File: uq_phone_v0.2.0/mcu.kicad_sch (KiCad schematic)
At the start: 41 parts, among them J6 Conn_ARM_SWD_TagConnect_TC2030, J7 559092474, J9 559092474, Q1 MMBT3904LP-7, Q2 MMBT3904LP-7, U17 TXU0204DTRR, U18 TXU0304DTRR, U19 TXU0104DTRR, U20 TXU0104DTRR, U5 TCA9509MRVHR, U6 STM32H723VGHx

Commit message: Regulator EN-controlled soft power latch prototype
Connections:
- net PWR_HOLD: now reaches U6.G5 (PB2)
- net PB_PWR renamed PWR_BUTTON_SENSE
- no-connect marks 16 -> 15

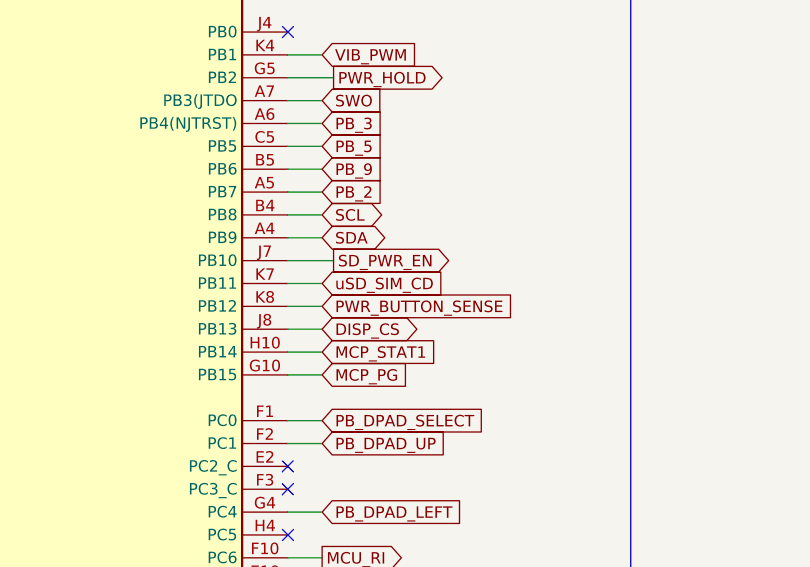
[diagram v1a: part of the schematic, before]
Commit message: Add shared tray detect for MCU and RC7620 SIM detection
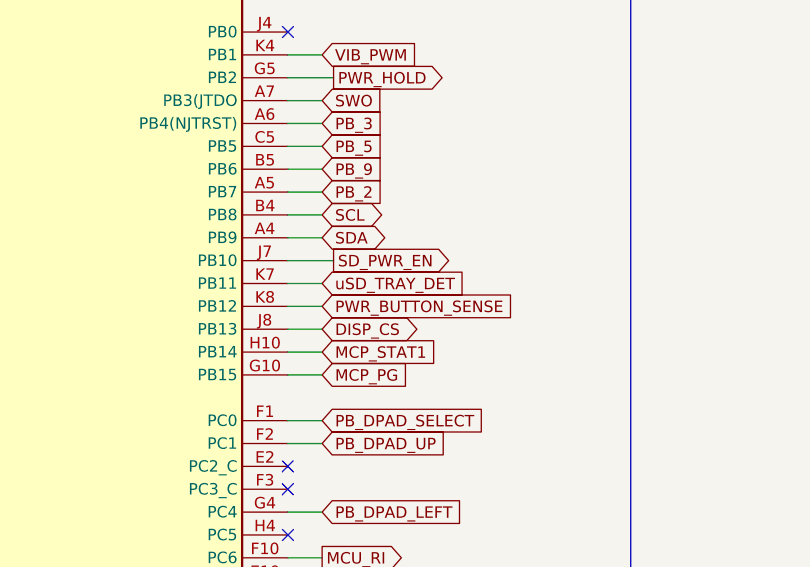
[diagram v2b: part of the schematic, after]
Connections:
- net uSD_SIM_CD renamed uSD_TRAY_DET

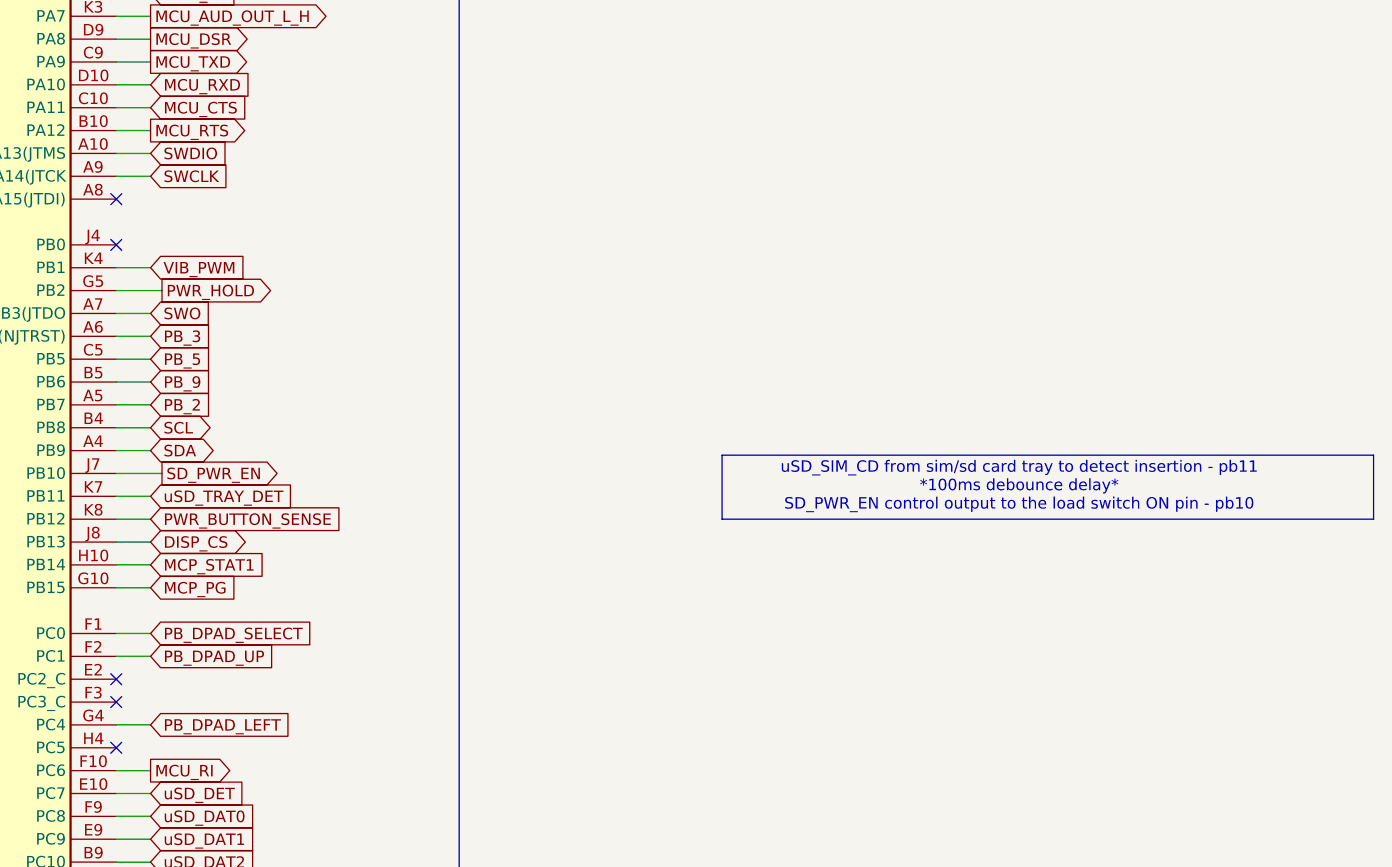
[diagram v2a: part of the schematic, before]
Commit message: Add soft power switch and update PCB design
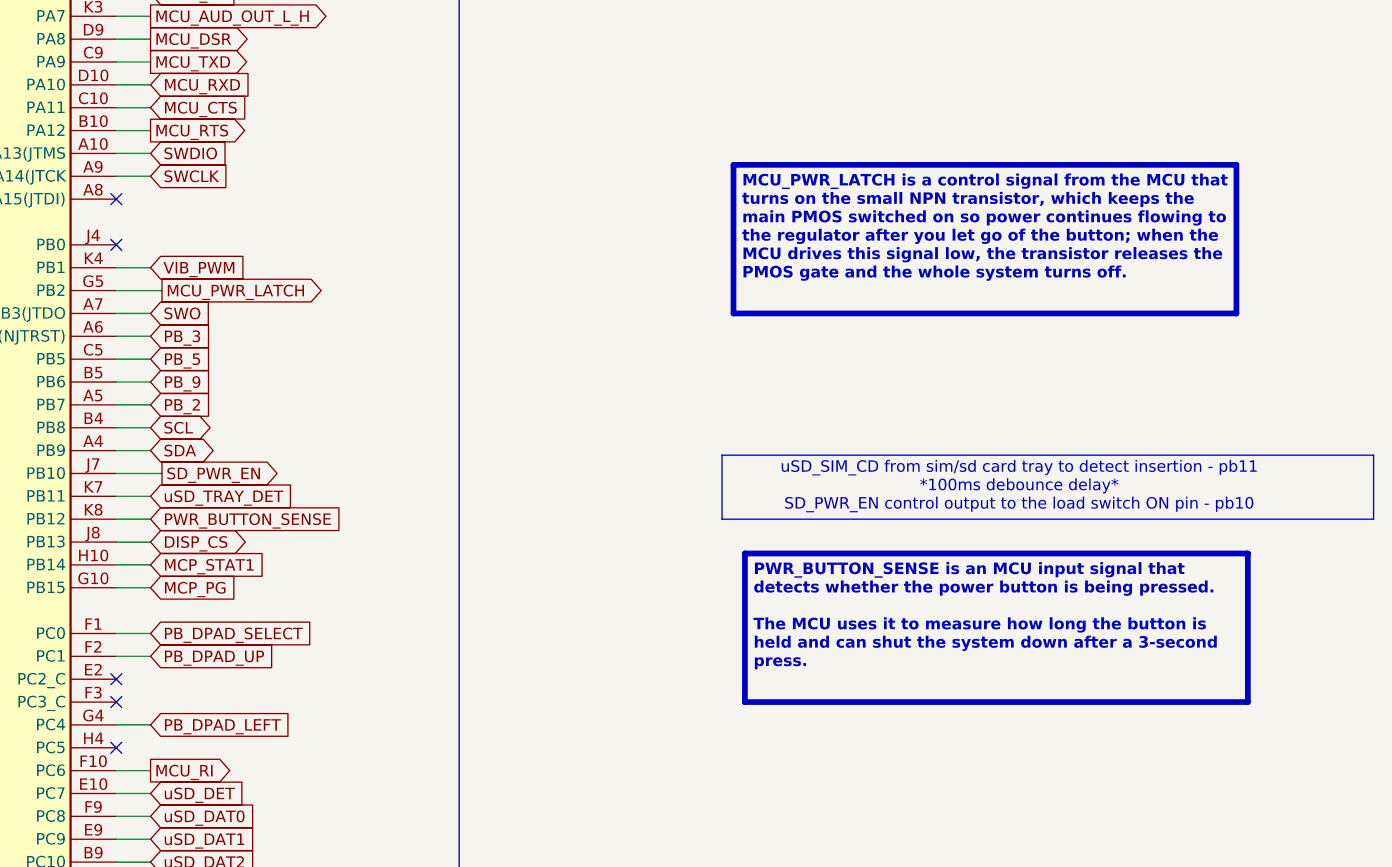
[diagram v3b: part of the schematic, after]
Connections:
- net PWR_HOLD renamed MCU_PWR_LATCH

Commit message: Fix KiCad libraries and update soft power circuit
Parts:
- Q2: footprint MMBT3904LP-7:DFN101X61X53-3N -> MMBT3904LP-7:MMBT3904LP7

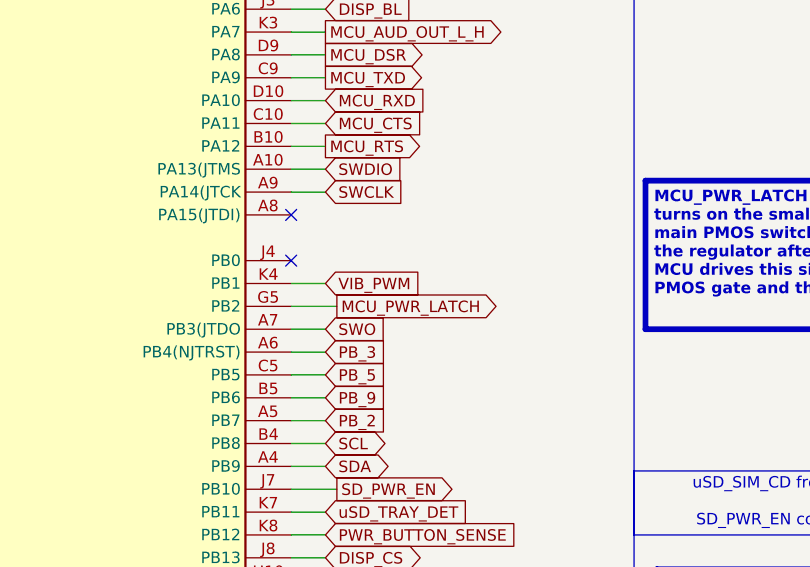
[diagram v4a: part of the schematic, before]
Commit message: Route soft power switch
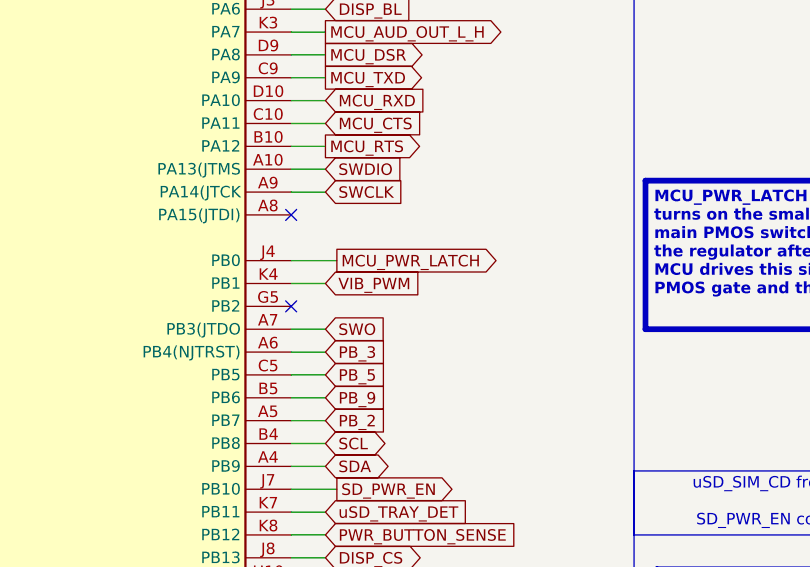
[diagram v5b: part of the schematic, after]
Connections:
- net MCU_PWR_LATCH: now also U6.J4 (PB0); no longer U6.G5 (PB2)

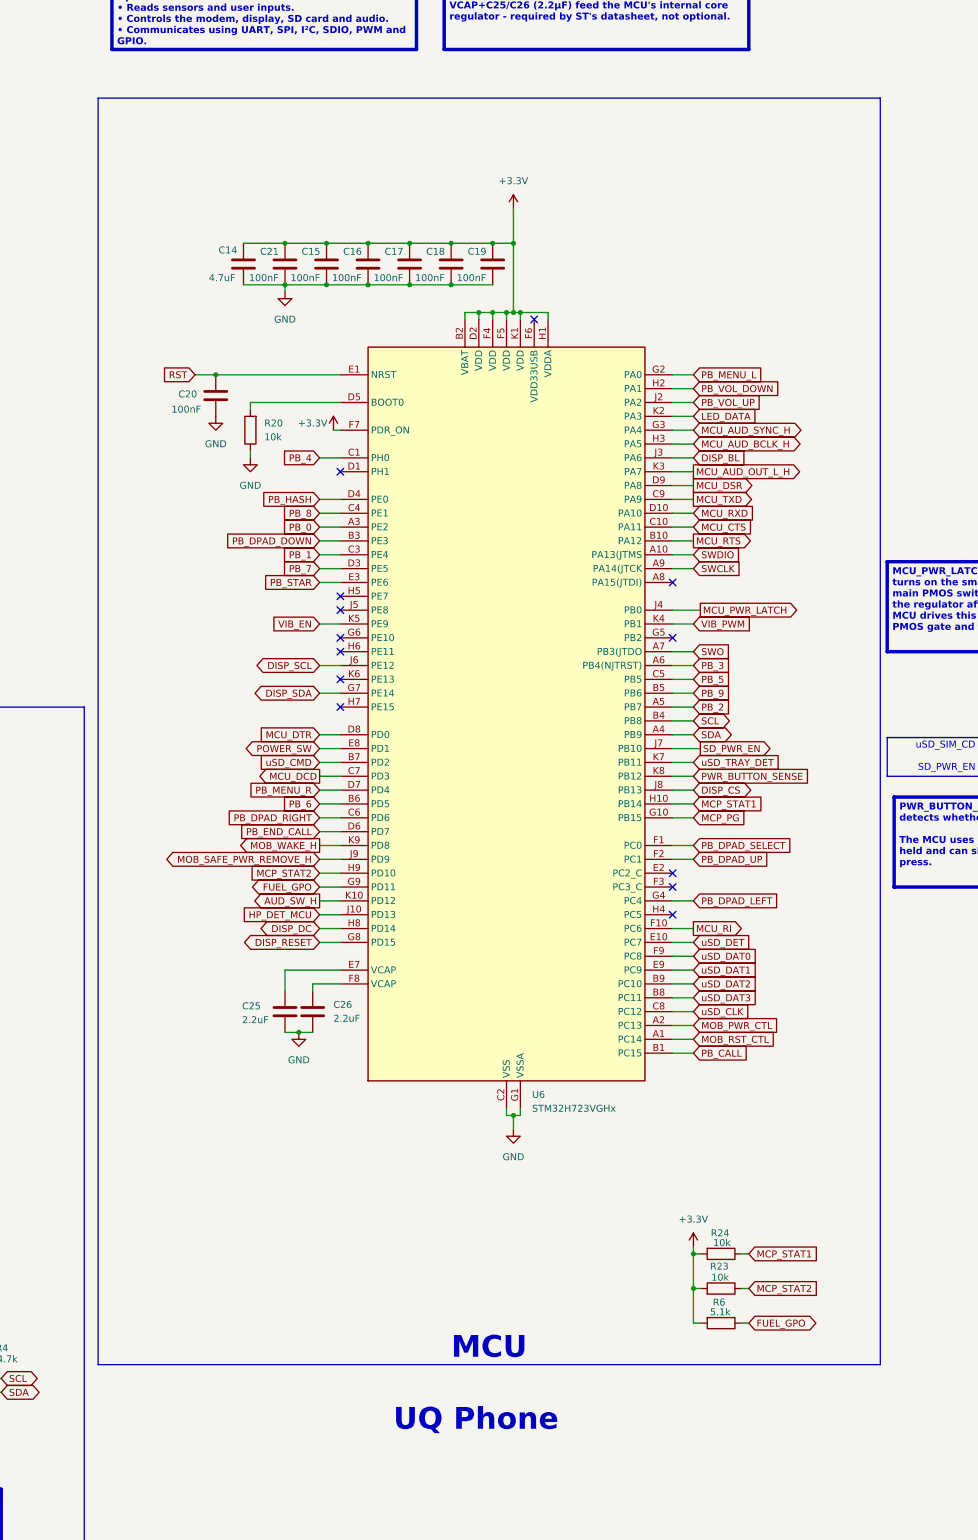
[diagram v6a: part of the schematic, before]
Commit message: Add GPIO expander and 16-bit FMC display schematic
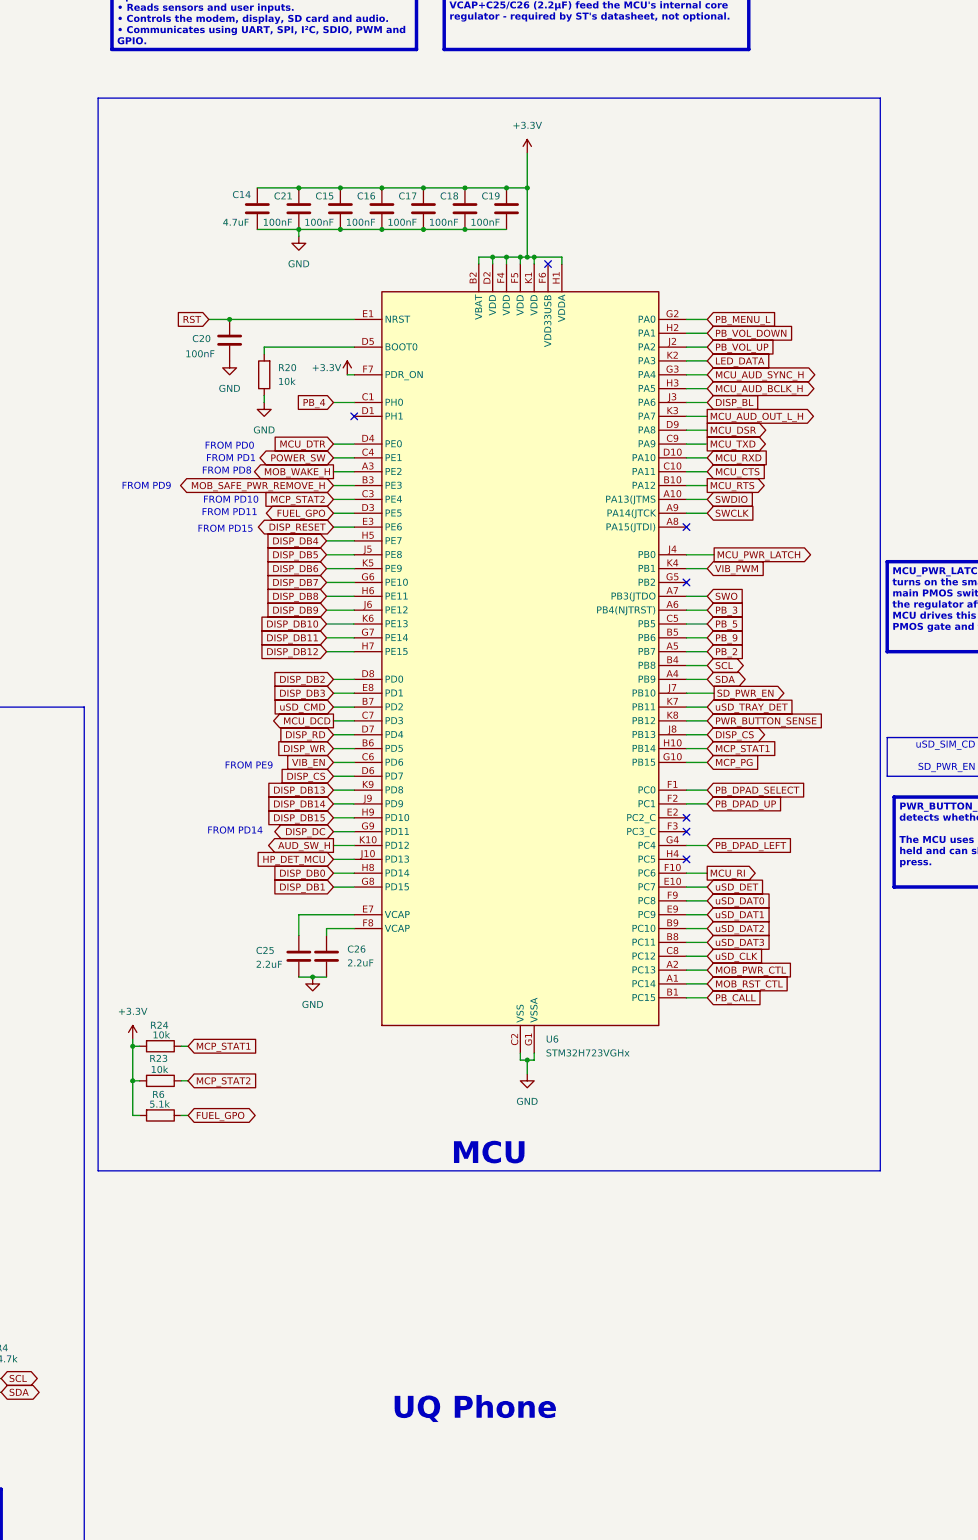
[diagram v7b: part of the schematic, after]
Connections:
- net PB_0 is gone; now on net MOB_WAKE_H: U6.A3 (PE2)
- net PB_1 is gone; now on net MCP_STAT2: U6.C3 (PE4)
- net PB_7 is gone; now on net FUEL_GPO: U6.D3 (PE5)
- net PB_8 is gone; now on net POWER_SW: U6.C4 (PE1)
- net PB_DPAD_DOWN is gone; now on net MOB_SAFE_PWR_REMOVE_H: U6.B3 (PE3)
- net PB_DPAD_RIGHT is gone; now on net VIB_EN: U6.C6 (PD6)
- net PB_END_CALL is gone; now on net DISP_CS: U6.D6 (PD7)
- net PB_HASH is gone; now on net MCU_DTR: U6.D4 (PE0)
- net PB_STAR is gone; now on net DISP_RESET: U6.E3 (PE6)
- net DISP_DC: now also U6.G9 (PD11); no longer U6.H8 (PD14)
- net DISP_RESET: no longer U6.G8 (PD15)
- net FUEL_GPO: no longer U6.G9 (PD11)
- net MCP_STAT2: no longer U6.H9 (PD10)
- net MCU_DTR: no longer U6.D8 (PD0)
- net MOB_SAFE_PWR_REMOVE_H: no longer U6.J9 (PD9)
- net MOB_WAKE_H: no longer U6.K9 (PD8)
- net POWER_SW: no longer U6.E8 (PD1)
- net VIB_EN: no longer U6.K5 (PE9)
- net DISP_DB7: now reaches U6.G6 (PE10)
- net DISP_DB4: now reaches U6.H5 (PE7)
- net DISP_DB8: now reaches U6.H6 (PE11)
- net DISP_DB12: now reaches U6.H7 (PE15)
- net DISP_DB5: now reaches U6.J5 (PE8)
- net DISP_DB10: now reaches U6.K6 (PE13)
- net DISP_SCL renamed DISP_DB9
- net DISP_SDA renamed DISP_DB11
- net PB_6 renamed DISP_WR
- net PB_MENU_R renamed DISP_RD
- new net DISP_DB0: U6.H8 (PD14)
- new net DISP_DB1: U6.G8 (PD15)
- new net DISP_DB13: U6.K9 (PD8)
- new net DISP_DB14: U6.J9 (PD9)
- new net DISP_DB15: U6.H9 (PD10)
- new net DISP_DB2: U6.D8 (PD0)
- new net DISP_DB3: U6.E8 (PD1)
- new net DISP_DB6: U6.K5 (PE9)
- no-connect marks 15 -> 9
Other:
- note added: "FROM PD0"
- note added: "FROM PD1"
- note added: "FROM PD10"
- note added: "FROM PD11"
- note added: "FROM PD14"
- note added: "FROM PD15"
- note added: "FROM PD8"
- note added: "FROM PD9"
- note added: "FROM PE9"
- moved on the sheet: C14, C15, C16, C17, C18, C19, C20, C21, C25, C26, R20, R23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
